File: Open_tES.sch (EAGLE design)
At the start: 57 parts, among them IC2 MAX232ECWES, IC3 4023D, IC4 LP2950CZ-5.0, IC5 OPA277U, IC6 LF444CM, IC7 PIC16F1937P, U1 TSR_1-2465, U2 ICL7660ACPAZ, X1 22-23-2041, X2 057-016-1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

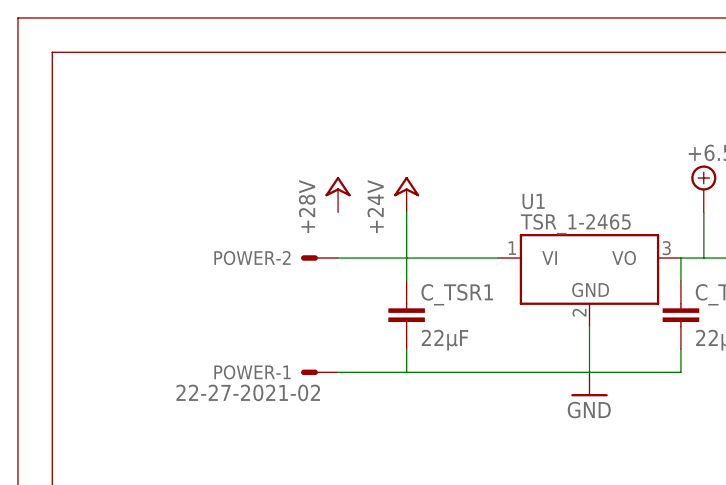
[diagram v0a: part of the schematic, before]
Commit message: removing supply 28+(not used)
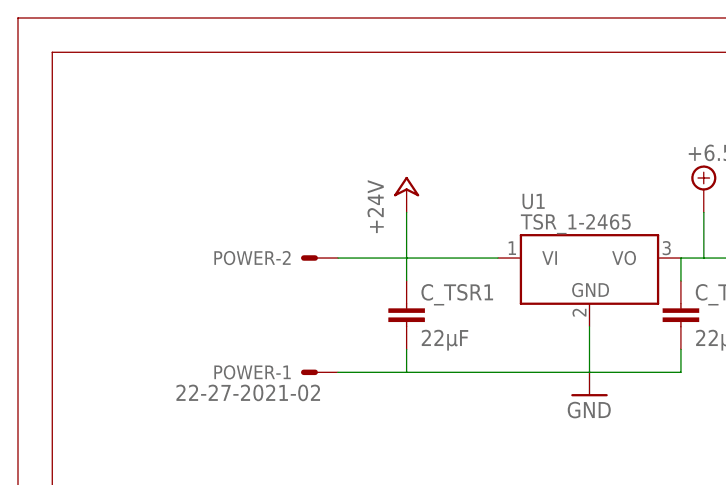
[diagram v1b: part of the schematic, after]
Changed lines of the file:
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@@
 <part name="FREE" library="pinhead" deviceset="PINHD-1X3" device=""/>
 <part name="GND15" library="supply1" deviceset="GND" device=""/>
-<part name="U$3" library="supply1" deviceset="+28V" device=""/>
 <part name="IC7" library="microchip" deviceset="PIC16F193*?" device="P" technology="7"/>
 <part name="SUPPLY6" library="supply2" deviceset="+5V/1" device="" value="+5V"/>
@@
 <instance part="FREE" gate="A" x="160.02" y="119.38" rot="R180"/>
 <instance part="GND15" gate="1" x="170.18" y="124.46"/>
-<instance part="U$3" gate="G$1" x="35.56" y="238.76"/>
 <instance part="IC7" gate="G$1" x="231.14" y="111.76"/>
 <instance part="SUPPLY6" gate="G$1" x="299.72" y="111.76" rot="R180"/>

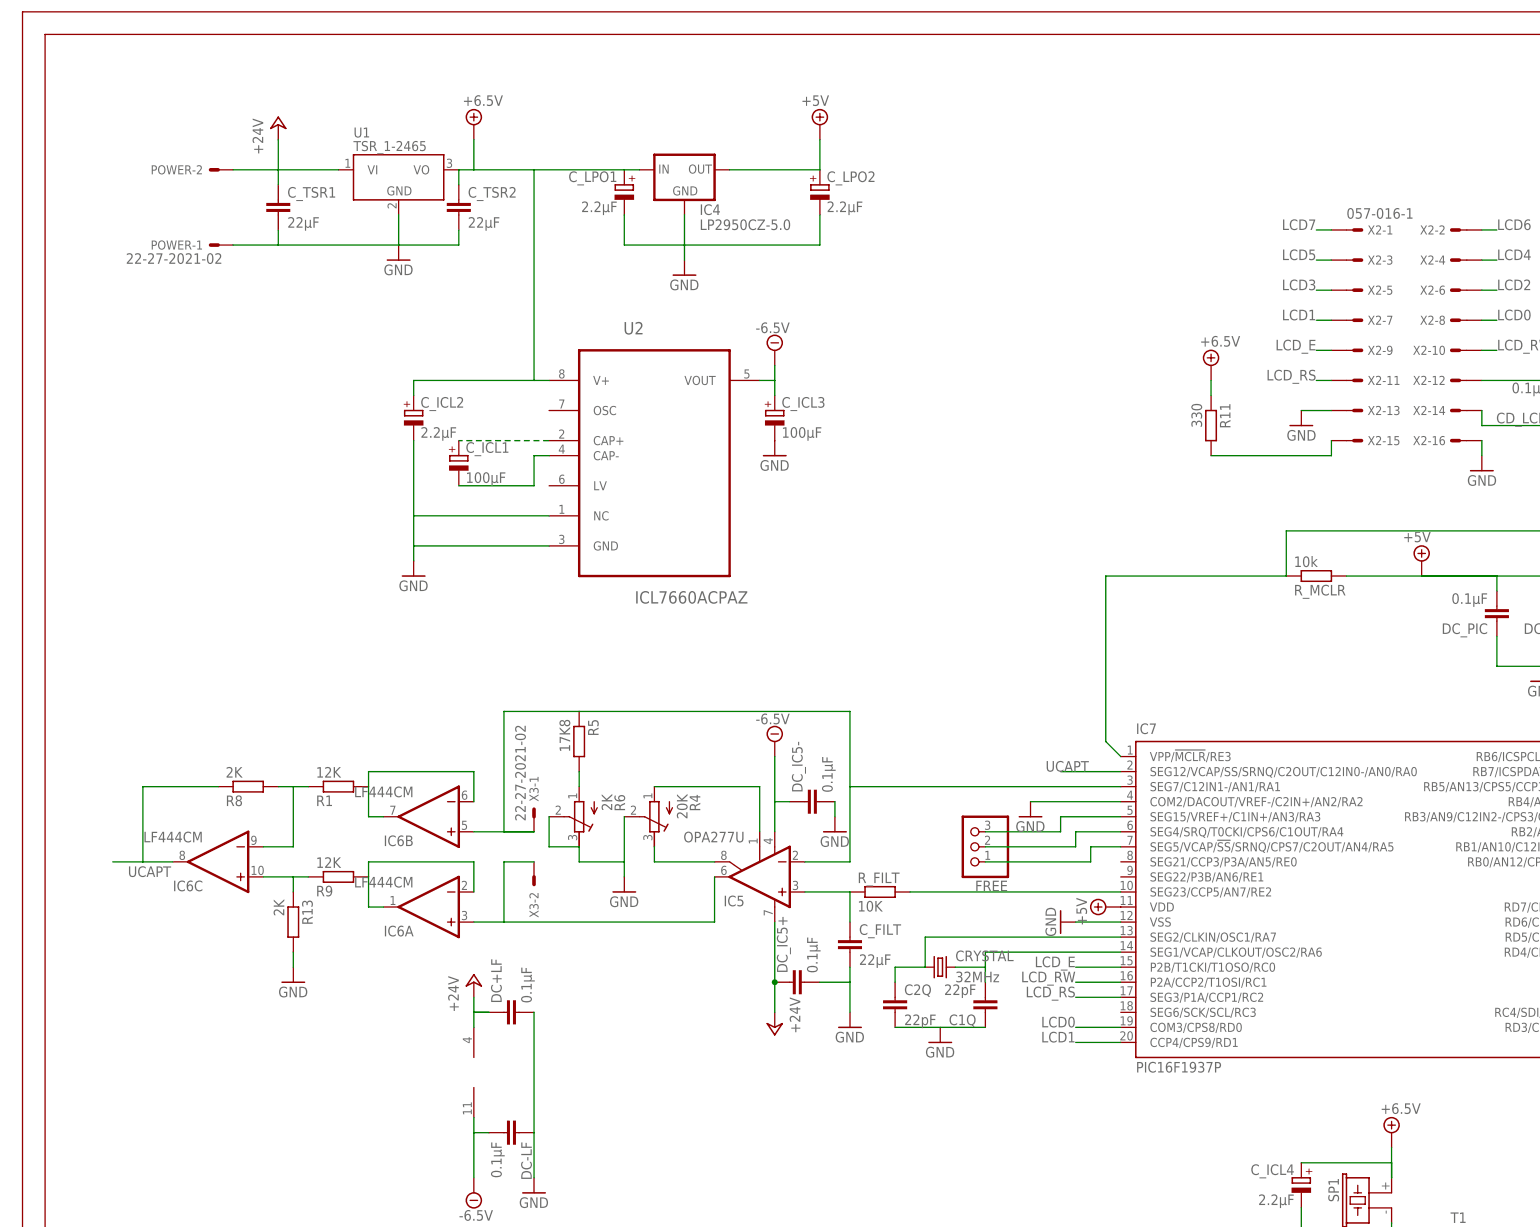
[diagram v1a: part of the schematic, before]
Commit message: replace TSR on the shematic by MIC2288 boost DC-DC
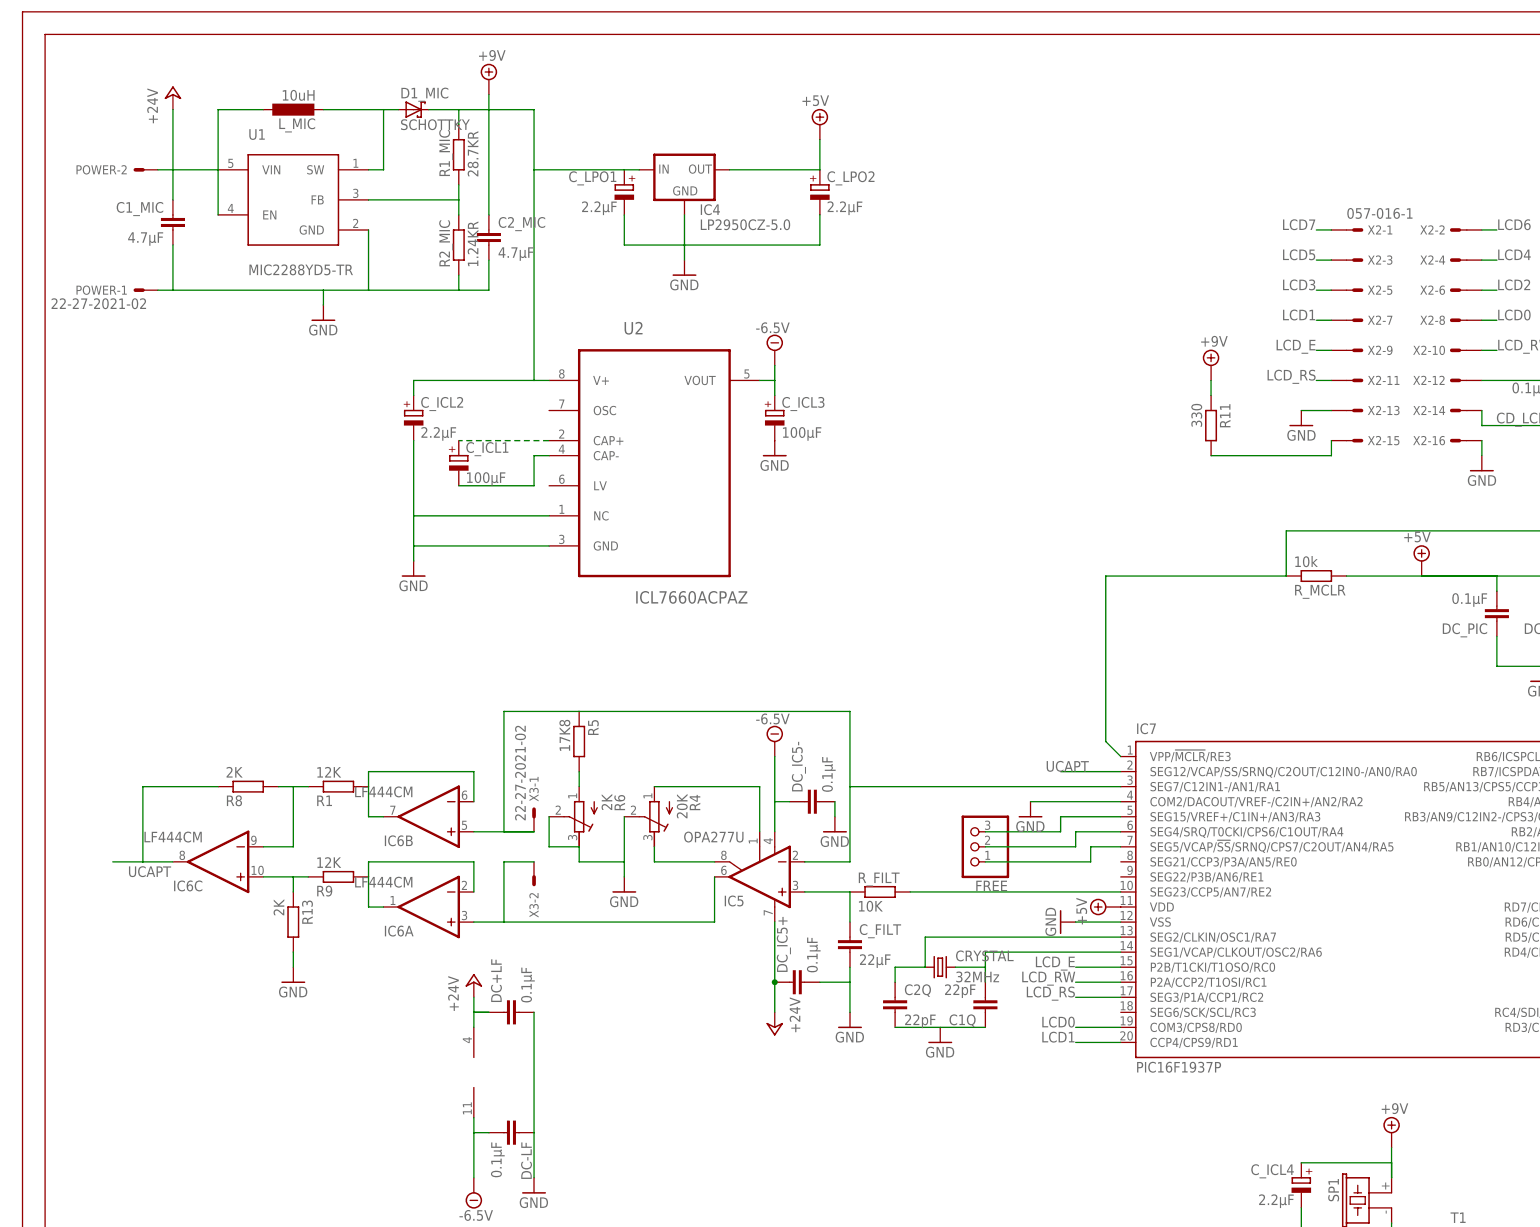
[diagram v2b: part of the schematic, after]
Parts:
- removed C_TSR1, C_TSR2: 22µF, rcl:C-EUC1206
- added C1_MIC, C2_MIC: 4.7µF, rcl:C-EUC0805
- added D1_MIC: SCHOTTKY, Open_tES:SCHOTTKY
- added L_MIC: 10uH, rcl:L-EUL2012C
- added R1_MIC: 28.7KR, rcl:R-EU_R0805
- added R2_MIC: 1.24KR, rcl:R-EU_R0805
- U1: value TSR_1-2465 -> MIC2288YD5-TR; device _traco_tsr-1:TSR_1-2465 -> Open_tES:MIC2288YD5-TR; OC_FARNELL 2451541 -> 2509929
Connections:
- removed net +7V: C_ICL2.+, C_ICL4.+, C_LPO1.+, C_TSR2.1, IC4.IN, R11.1, SP1.1, U1.VO, U2.V+
- new net +9V: C2_MIC.1, C_ICL2.+, C_ICL4.+, C_LPO1.+, D1_MIC.C, IC4.IN, R11.1, R1_MIC.2, SP1.1, U2.V+
- new net N$10: R1_MIC.1, R2_MIC.2, U1.FB
- new net N$35: D1_MIC.A, L_MIC.2, U1.SW
- net +24V: now also C1_MIC.1, L_MIC.1, U1.EN, U1.VIN; no longer C_TSR1.1, U1.VI
- net GND: now also C1_MIC.2, C2_MIC.2, R2_MIC.1; no longer C_TSR1.2, C_TSR2.2
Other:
- moved on the sheet: POWER-1, POWER-2

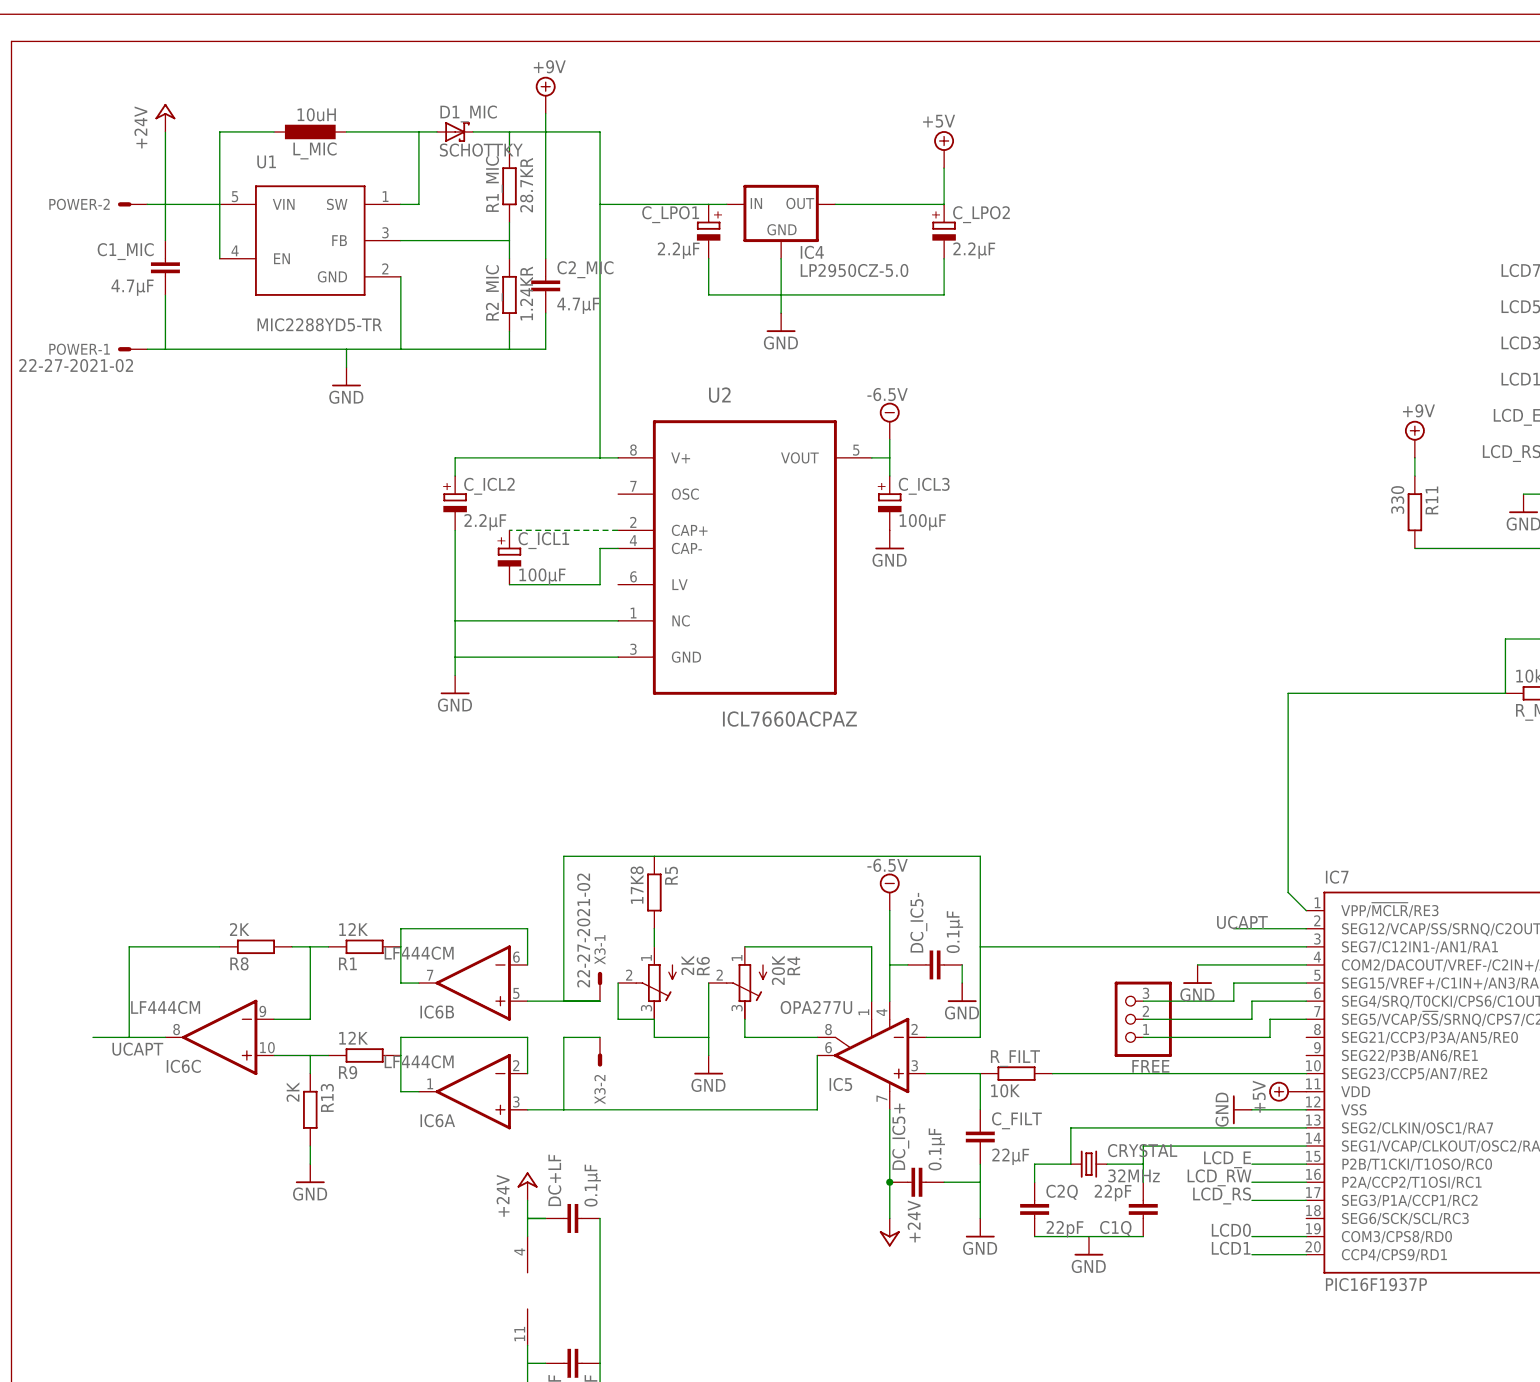
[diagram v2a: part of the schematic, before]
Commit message: backlight resistor for 9V supply
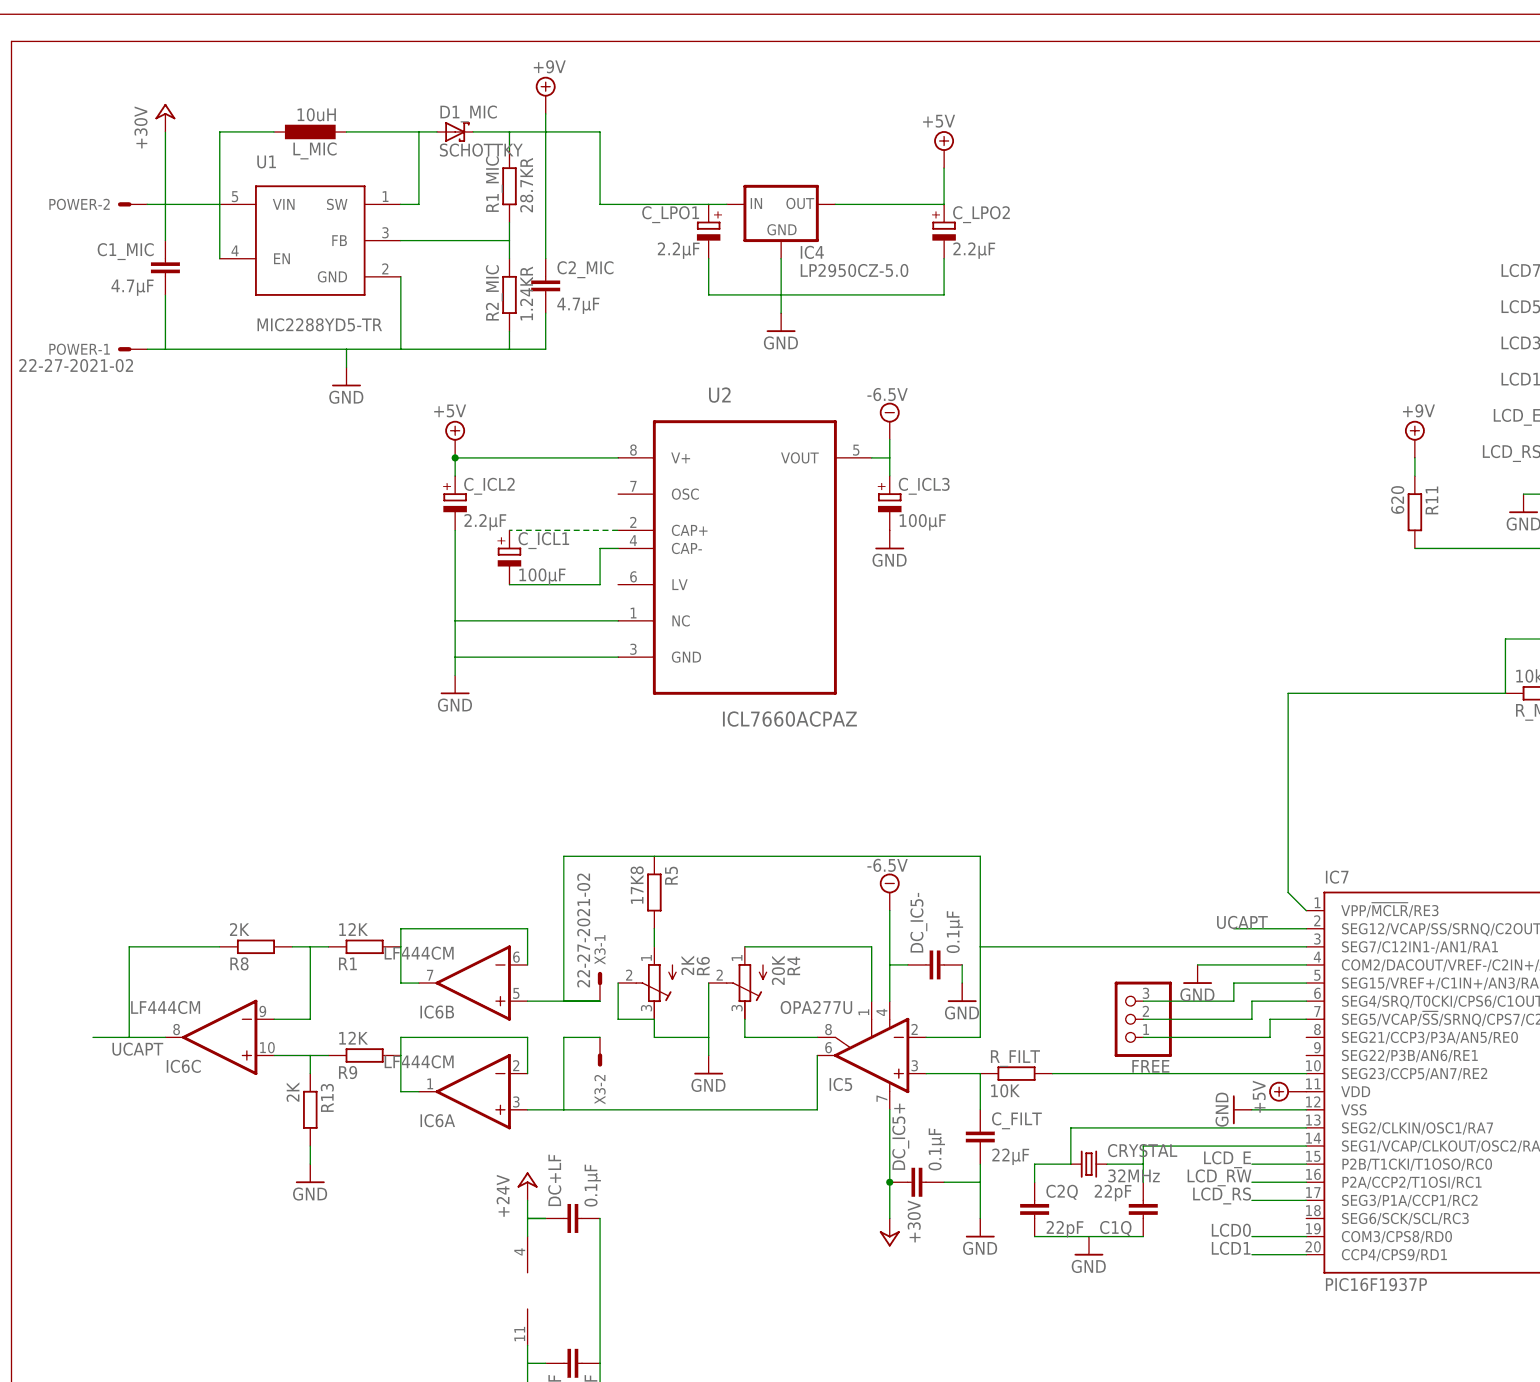
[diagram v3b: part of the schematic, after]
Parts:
- R11: value 330 -> 620; OC_FARNELL 9339418 -> 2329960
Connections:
- net +5V/1: now also C_ICL2.+, U2.V+
- net +9V: no longer C_ICL2.+, U2.V+
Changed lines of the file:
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@@
 </part>
 <part name="GND9" library="supply1" deviceset="GND" device=""/>
-<part name="P+8" library="supply1" deviceset="+24V" device=""/>
+<part name="P+8" library="supply1" deviceset="+24V" device="" value="+30V"/>
 <part name="R_BUZZ" library="rcl" deviceset="R-EU_" device="R0805" value="2K7">
 <attribute name="OC_FARNELL" value="9339361"/>
@@
 <part name="GND12" library="supply1" deviceset="GND" device=""/>
 <part name="GND14" library="supply1" deviceset="GND" device=""/>
-<part name="R11" library="rcl" deviceset="R-EU_" device="0204/7" value="330">
-<attribute name="OC_FARNELL" value="9339418"/>
+<part name="R11" library="rcl" deviceset="R-EU_" device="0204/7" value="620">
+<attribute name="OC_FARNELL" value="2329960"/>
 </part>
 <part name="GND29" library="supply1" deviceset="GND" device=""/>
@@
 <attribute name="OC_FARNELL" value="8766983"/>
 </part>
-<part name="P+1" library="supply1" deviceset="+24V" device=""/>
+<part name="P+1" library="supply1" deviceset="+24V" device="" value="+30V"/>
 <part name="SUPPLY13" library="supply2" deviceset="+9V" device="" value="+9V"/>
 <part name="DC_PIC1" library="rcl" deviceset="C-EU" device="C0805" value="0.1µF">
@@
 <attribute name="OC_FARNELL" value="1469389"/>
 </part>
+<part name="SUPPLY16" library="supply2" deviceset="+5V/1" device="" value="+5V"/>
 </parts>
 <sheets>
@@
 <attribute name="OC_FARNELL" x="66.04" y="243.84" size="1.778" layer="96" display="off"/>
 </instance>
+<instance part="SUPPLY16" gate="G$1" x="66.04" y="200.66"/>
 </instances>
 <busses>
@@
 <pinref part="SUPPLY7" gate="G$1" pin="+5V/1"/>
 </segment>
+<segment>
+<pinref part="U2" gate="A" pin="V+"/>
+<wire x1="66.04" y1="198.12" x2="88.9" y2="198.12" width="0.1524" layer="91"/>
+<pinref part="C_ICL2" gate="G$1" pin="+"/>
+<wire x1="66.04" y1="195.58" x2="66.04" y2="198.12" width="0.1524" layer="91"/>
+<pinref part="SUPPLY16" gate="G$1" pin="+5V/1"/>
+<junction x="66.04" y="198.12"/>
+</segment>
 </net>
 <net name="N$32" class="0">
@@
 <wire x1="78.74" y1="243.84" x2="86.36" y2="243.84" width="0.1524" layer="91"/>
 <wire x1="86.36" y1="243.84" x2="86.36" y2="233.68" width="0.1524" layer="91"/>
-<pinref part="U2" gate="A" pin="V+"/>
 <wire x1="86.36" y1="233.68" x2="101.6" y2="233.68" width="0.1524" layer="91"/>
-<pinref part="C_ICL2" gate="G$1" pin="+"/>
-<wire x1="66.04" y1="195.58" x2="66.04" y2="198.12" width="0.1524" layer="91"/>
-<wire x1="66.04" y1="198.12" x2="86.36" y2="198.12" width="0.1524" layer="91"/>
-<wire x1="86.36" y1="198.12" x2="88.9" y2="198.12" width="0.1524" layer="91"/>
-<wire x1="86.36" y1="233.68" x2="86.36" y2="198.12" width="0.1524" layer="91"/>
 <wire x1="101.6" y1="233.68" x2="104.14" y2="233.68" width="0.1524" layer="91"/>
 <pinref part="R1_MIC" gate="G$1" pin="2"/>
